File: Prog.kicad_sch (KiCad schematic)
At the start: 19 parts, among them J2 JTAG, J3 microUSB, Q1 MMBT3904, U12 CH340G, Y1 12M

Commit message: idk
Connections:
- net +3V3: no longer U12.12 (~{DCD})
- net GND: now also U12.12 (~{DCD})
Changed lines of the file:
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@@
-	)
-	(junction
-		(at 210.82 64.77)
-		(diameter 0)
-		(color 0 0 0 0)
 	)
 	(junction
@@
 	(wire
 		(pts
-			(xy 205.74 64.77) (xy 210.82 64.77)
+			(xy 203.2 62.23) (xy 210.82 62.23)
 		)
 		(stroke
@@
 	(wire
 		(pts
-			(xy 210.82 62.23) (xy 210.82 64.77)
-		)
-		(stroke
-			(width 0)
-			(type default)
-		)
-	)
-	(wire
-		(pts
 			(xy 219.71 147.32) (xy 229.87 147.32)
 		)
@@
 		(pts
 			(xy 224.79 93.98) (xy 222.25 93.98)
+		)
+		(stroke
+			(width 0)
+			(type default)
+		)
+	)
+	(wire
+		(pts
+			(xy 203.2 64.77) (xy 210.82 64.77)
 		)
 		(stroke
@@
 	(symbol
 		(lib_id "power:+3V3")
-		(at 205.74 64.77 0)
+		(at 203.2 62.23 0)
 		(unit 1)
 		(exclude_from_sim no)
@@
 		(dnp no)
 		(property "Reference" "#PWR022"
-			(at 205.74 68.58 0)
+			(at 203.2 66.04 0)
 			(effects
 				(font
@@
 		)
 		(property "Value" "+3V3"
-			(at 205.74 60.96 0)
+			(at 203.2 58.42 0)
 			(effects
 				(font
@@
 		)
 		(property "Footprint" ""
-			(at 205.74 64.77 0)
+			(at 203.2 62.23 0)
 			(effects
 				(font
@@
 		)
 		(property "Datasheet" ""
-			(at 205.74 64.77 0)
+			(at 203.2 62.23 0)
 			(effects
 				(font
@@
 		)
 		(property "Description" ""
-			(at 205.74 64.77 0)
+			(at 203.2 62.23 0)
 			(effects
 				(font
@@
 					(unit 1)
 				)
+			)
+		)
+	)
+	(symbol
+		(lib_id "power:GND")
+		(at 203.2 64.77 0)
+		(mirror y)
+		(unit 1)
+		(exclude_from_sim no)
+		(in_bom yes)
+		(on_board yes)
+		(dnp no)
+		(property "Reference" "#PWR041"
+			(at 203.2 71.12 0)
+			(effects
+				(font
+					(size 1.27 1.27)
+				)
+				(hide yes)
+			)
+		)
+		(property "Value" "GND"
+			(at 203.2 68.58 0)
+			(effects
+				(font
+					(size 1.27 1.27)
+				)
+			)
+		)
+		(property "Footprint" ""
+			(at 203.2 64.77 0)
+			(effects
+				(font
+					(size 1.27 1.27)
+				)
+				(hide yes)
+			)
+		)
+		(property "Datasheet" ""
+			(at 203.2 64.77 0)
+			(effects
+				(font
+					(size 1.27 1.27)
+				)
+				(hide yes)
+			)
+		)
+		(property "Description" ""
+			(at 203.2 64.77 0)
+			(effects
+				(font
+					(size 1.27 1.27)
+				)
+				(hide yes)
+			)
+		)
+		(pin "1"
+		)
+		(instances
+			(project "WarpSE"
+				(path "/a5be2cb8-c68d-4180-8412-69a6b4c5b1d4/00000000-0000-0000-0000-000061aa52c4"
+					(reference "#PWR041")
+					(unit 1)
+				)

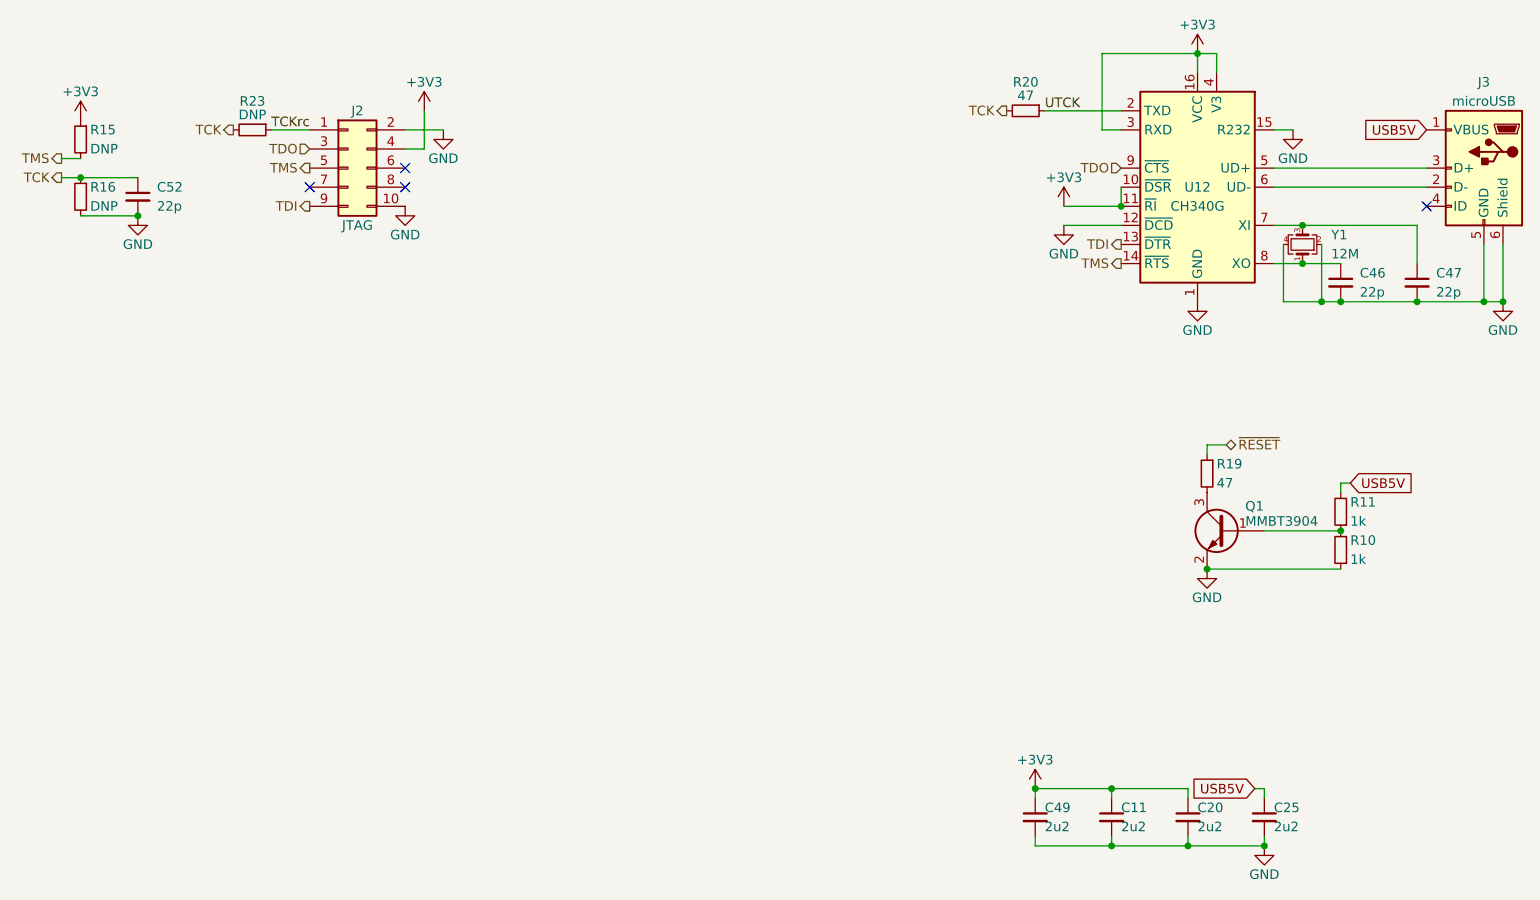
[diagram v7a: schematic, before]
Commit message: Before remove first clock input buffer
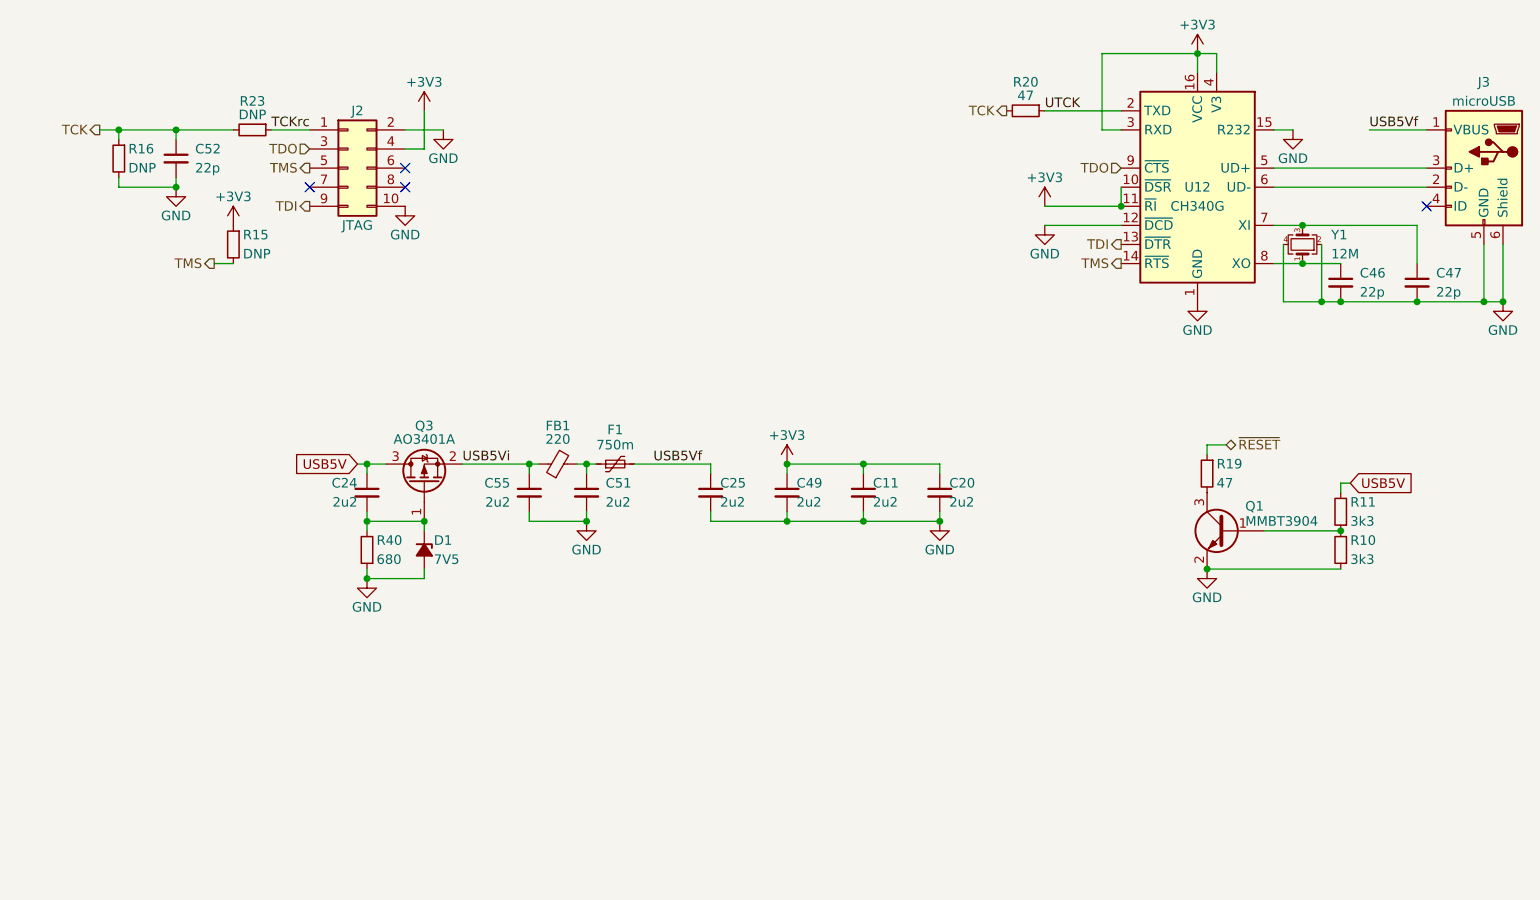
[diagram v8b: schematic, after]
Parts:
- added C24, C51, C55: 2u2, stdpads:C_0603, symbol Device:C_Small
- added D1: 7V5, stdpads:D_SOD-323, symbol Device:D_Zener_Small_Filled
- added F1: 750m, stdpads:BelFuse_1206, symbol Device:Polyfuse_Small
- added FB1: 220, stdpads:C_0805, symbol Device:FerriteBead_Small
- added Q3: AO3401A, stdpads:SOT-23, symbol Device:Q_PMOS_GSD
- added R40: 680, stdpads:R_0805, symbol Device:R_Small
- R10, R11: value 1k -> 3k3
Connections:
- net GND: now also C51.2, C55.2, D1.2 (A), R40.1
- net USB5V: now also C24.1, Q3.3 (D); no longer C25.1, J3.1 (VBUS)
- new net: C24.2, D1.1 (K), Q3.1 (G), R40.2
- new net: C51.1, F1.1, FB1.2
- new net USB5Vf: C25.1, F1.2, J3.1 (VBUS)
- new net USB5Vi: C55.1, FB1.1, Q3.2 (S)
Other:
- moved on the sheet: C11, C20, C25, C49, C52, R15, R16
